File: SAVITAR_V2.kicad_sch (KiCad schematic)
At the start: 71 parts, among them IC1 CD4051BM_TR, IC2 CD4051BM_TR, J2 FH34SRJ-12S-0.5SH_50_

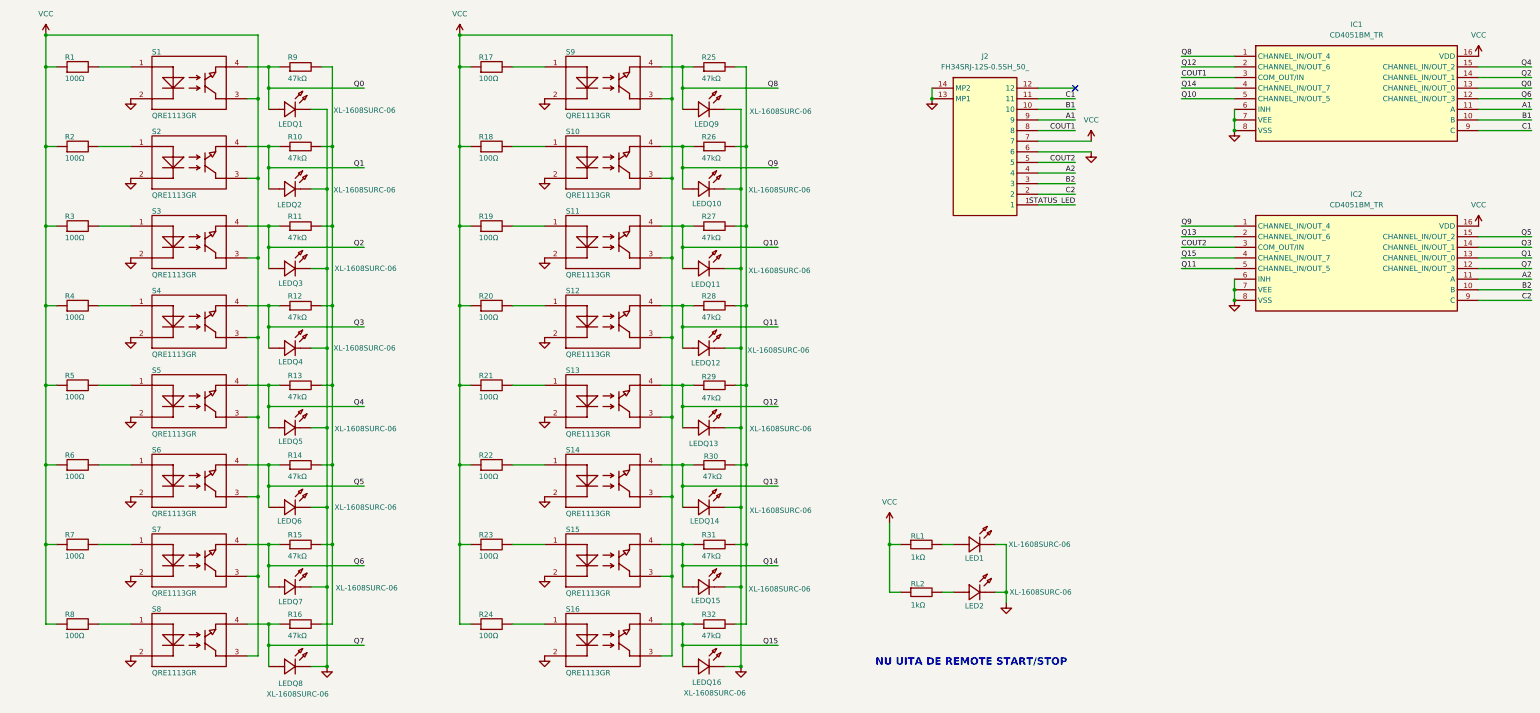
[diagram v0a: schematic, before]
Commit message: Added Decoder 3x8 (74HC238D) and 8 NMOS array (TBD62083AFNG) for driving the LEDs in pairs of 2 (±40 mA) only when they are read.
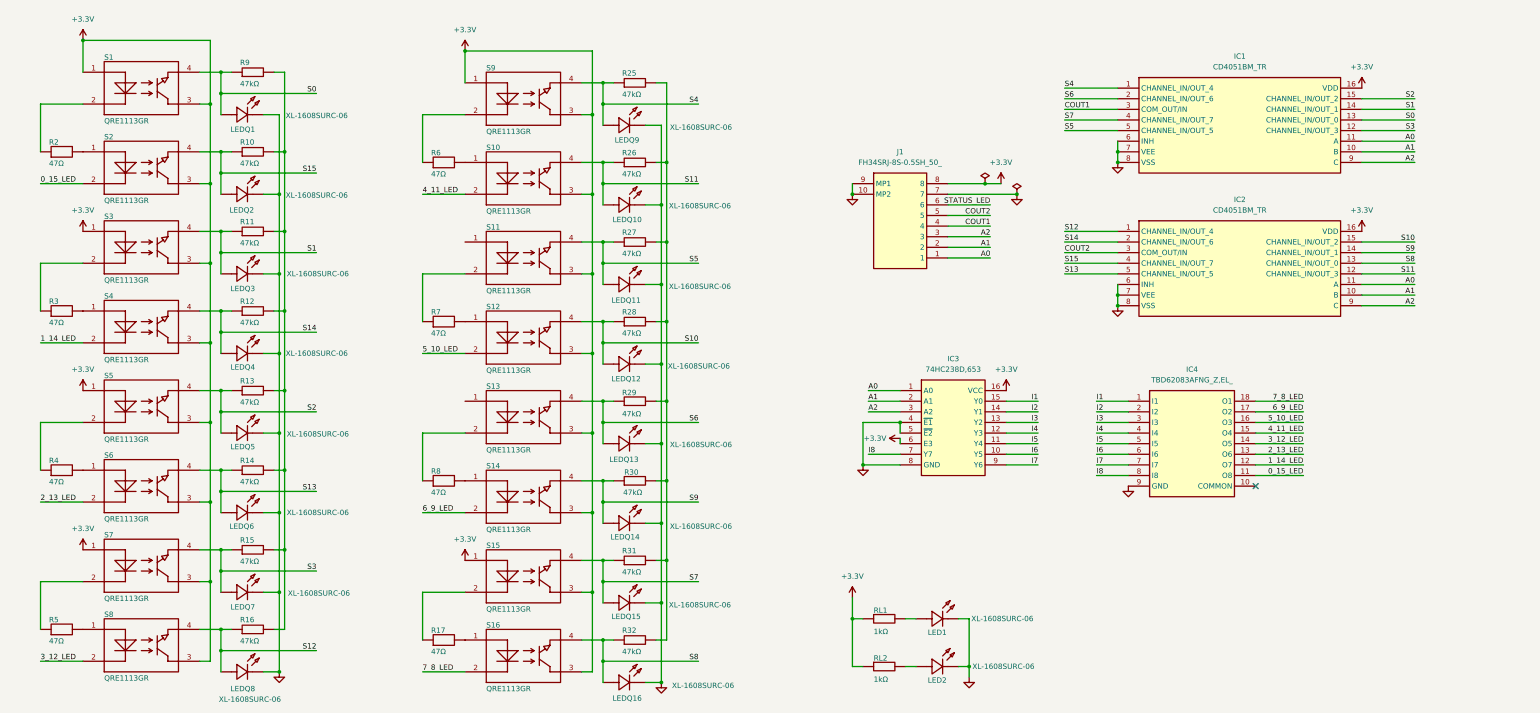
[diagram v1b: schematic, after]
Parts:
- removed J2: FH34SRJ-12S-0.5SH_50_, FH34SRJ-12S-0.5SH_50_:FH34SRJ12S05SH50, symbol FH34SRJ-12S-0_5SH_50_:FH34SRJ-12S-0.5SH_50_
- removed R1, R18, R19, R20, R21, R22, R23, R24: 100Ω, Resistor_SMD:R_0603_1608Metric, symbol SAVITAR_V2-altium-import:root_0_SCR0603J100R_
- added IC3: 74HC238D,653, 74HC238D653, symbol SAVITAR:74HC238D,653
- added IC4: TBD62083AFNG_Z,EL_, SOP65P640X155-18N, symbol SAVITAR:TBD62083AFNG_Z,EL_
- added J1: FH34SRJ-8S-0.5SH_50_, FH34SRJ8S05SH50, symbol SAVITAR:FH34SRJ-8S-0.5SH_50_
- R17, R2, R3, R4, R5, R6, R7, R8: value 100Ω -> 47Ω
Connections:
- net B1 is gone; now on net A1: IC1.10 (B)
- net B2 is gone; now on net A1: IC2.10 (B)
- net C1 is gone; now on net A2: IC1.9 (C)
- net C2 is gone; now on net A2: IC2.9 (C)
- net A1: now also IC3.2 (A1), J1.2; no longer IC1.11 (A)
- net A2: now also IC3.3 (A2), J1.3; no longer IC2.11 (A)
- net COUT1: now also J1.4
- net COUT2: now also J1.5
- net GND: now also IC3.4 (~{E1}), IC3.5 (~{E2}), IC3.8 (GND), IC4.9 (GND), J1.10 (MP2), J1.7, J1.9 (MP1); no longer S1.2, S10.2, S11.2, S12.2, S13.2, S14.2, S15.2, S16.2, S2.2, S3.2, S4.2, S5.2, S6.2, S7.2, S8.2, S9.2
- net STATUS_LED: now also J1.6
- net at R10.2, R11.2, R12.2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: now also R3.2; no longer R6.2
- net at R17.2: now also S16.1; no longer S9.1
- net at R5.2: now also S8.1; no longer S5.1
- net at R7.2: now also S12.1; no longer S7.1
- net +3.3V: now reaches S3.1
- net +3.3V: now also IC1.16 (VDD), IC2.16 (VDD), RL1.1, RL2.1, S1.1, S1.3, S10.3, S11.3, S12.3, S13.3, S14.3, S15.1, S15.3, S16.3, S2.3, S3.3, S4.3, S5.1, S5.3, S6.3, S7.1, S7.3, S8.3, S9.1, S9.3, IC3.16 (VCC), IC3.6 (E3), J1.8; no longer R3.2
- net at R8.2: now also S14.1; no longer S8.1
- net at S10.1: now also R6.2
- net Q0 renamed S0
- net Q1 renamed S15
- net S15: now also IC2.4 (CHANNEL_IN/OUT_7); no longer IC2.13 (CHANNEL_IN/OUT_0)
- net Q10 renamed S5
- net Q11 renamed S10
- net S10: now also IC2.15 (CHANNEL_IN/OUT_2); no longer IC2.5 (CHANNEL_IN/OUT_5)
- net Q12 renamed S6
- net Q13 renamed S9
- net S9: now also IC2.14 (CHANNEL_IN/OUT_1); no longer IC2.2 (CHANNEL_IN/OUT_6)
- net Q14 renamed S7
- net Q15 renamed S8
- net S8: now also IC2.13 (CHANNEL_IN/OUT_0); no longer IC2.4 (CHANNEL_IN/OUT_7)
- net Q2 renamed S1
- net Q3 renamed S14
- net S14: now also IC2.2 (CHANNEL_IN/OUT_6); no longer IC2.14 (CHANNEL_IN/OUT_1)
- net Q4 renamed S2
- net Q5 renamed S13
- net S13: now also IC2.5 (CHANNEL_IN/OUT_5); no longer IC2.15 (CHANNEL_IN/OUT_2)
- net Q6 renamed S3
- net Q7 renamed S12
- net S12: now also IC2.1 (CHANNEL_IN/OUT_4); no longer IC2.12 (CHANNEL_IN/OUT_3)
- net Q8 renamed S4
- net Q9 renamed S11
- net S11: now also IC2.12 (CHANNEL_IN/OUT_3); no longer IC2.1 (CHANNEL_IN/OUT_4)
- removed net VCC: IC1.16 (VDD), IC2.16 (VDD), R17.1, R2.1, R3.1, R4.1, R5.1, R6.1, R7.1, R8.1, RL1.1, RL2.1, S1.3, S10.3, S11.3, S12.3, S13.3, S14.3, S15.3, S16.3, S2.3, S3.3, S4.3, S5.3, S6.3, S7.3, S8.3, S9.3
- new net: R3.1, S3.2
- new net: R6.1, S9.2
- new net: R17.1, S15.2
- new net: R4.1, S5.2
- new net: R5.1, S7.2
- new net: R2.1, S1.2
- new net: R7.1, S11.2
- new net: R8.1, S13.2
- new net 0_15_LED: IC4.11 (O8), S2.2
- new net 1_14_LED: IC4.12 (O7), S4.2
- new net 2_13_LED: IC4.13 (O6), S6.2
- new net 3_12_LED: IC4.14 (O5), S8.2
- new net 4_11_LED: IC4.15 (O4), S10.2
- new net 5_10_LED: IC4.16 (O3), S12.2
- new net 6_9_LED: IC4.17 (O2), S14.2
- new net 7_8_LED: IC4.18 (O1), S16.2
- new net A0: IC1.11 (A), IC2.11 (A), IC3.1 (A0), J1.1
- new net I1: IC3.15 (Y0), IC4.1 (I1)
- new net I2: IC3.14 (Y1), IC4.2 (I2)
- new net I3: IC3.13 (Y2), IC4.3 (I3)
- new net I4: IC3.12 (Y3), IC4.4 (I4)
- new net I5: IC3.11 (Y4), IC4.5 (I5)
- new net I6: IC3.10 (Y5), IC4.6 (I6)
- new net I7: IC3.9 (Y6), IC4.7 (I7)
- new net I8: IC3.7 (Y7), IC4.8 (I8)
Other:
- note removed: "NU UITA DE REMOTE START/STOP"
- moved on the sheet: IC1, IC2, LED1, LED2, LEDQ1, LEDQ10, LEDQ11, LEDQ12, LEDQ13, LEDQ14, LEDQ15, LEDQ16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

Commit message: Changed schematic structure. Separated sensor array from PD processing and motor control. Sensor schematic is finished. Moving to MCU wiring. All project symbols and footprints are under SAVITAR name for easier finding. Add appropriate TAG.
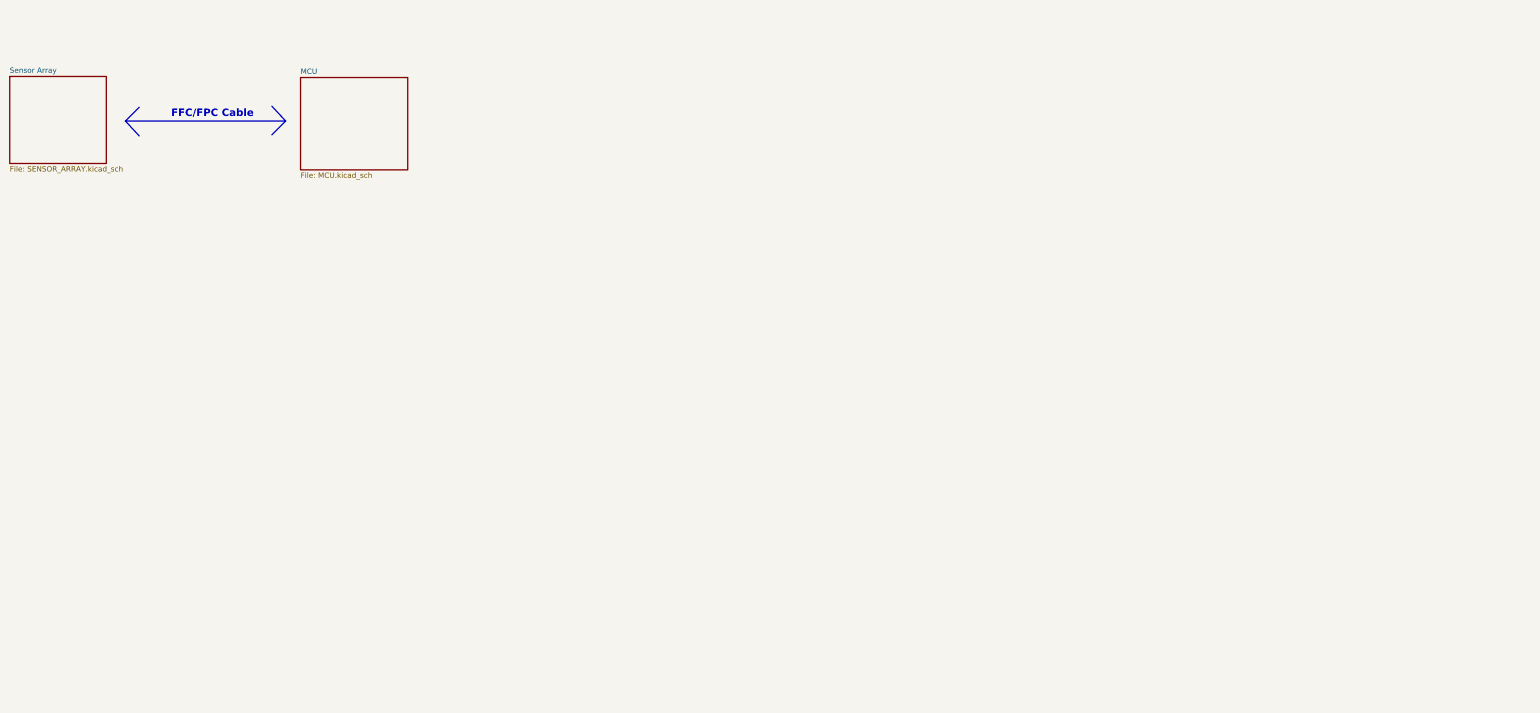
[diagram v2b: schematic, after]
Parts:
- removed IC1, IC2: CD4051BM_TR, CD4051BM_TR:SOIC127P602X182-16N, symbol CD4051BM_TR:CD4051BM_TR
- removed IC3: 74HC238D,653, 74HC238D653, symbol SAVITAR:74HC238D,653
- removed IC4: TBD62083AFNG_Z,EL_, SOP65P640X155-18N, symbol SAVITAR:TBD62083AFNG_Z,EL_
- removed J1: FH34SRJ-8S-0.5SH_50_, FH34SRJ8S05SH50, symbol SAVITAR:FH34SRJ-8S-0.5SH_50_
- removed LED1, LED2, LEDQ1, LEDQ10, LEDQ11, LEDQ12, LEDQ13, LEDQ14, LEDQ15, LEDQ16, LEDQ2, LEDQ3, LEDQ4, LEDQ5, LEDQ6, LEDQ7, LEDQ8, LEDQ9: XL-1608SURC-06, LED_SMD:LED_0603_1608Metric, symbol SAVITAR_V2-altium-import:root_0_mirrored_XL-1608SURC-06_
- removed R10, R11, R12, R13, R14, R15, R16, R25, R26, R27, R28, R29, R30, R31, R32, R9: 47kΩ, Resistor_SMD:R_0603_1608Metric, symbol SAVITAR_V2-altium-import:root_0_AC0603FR-0747KL_
- removed R17, R2, R3, R4, R5, R6, R7, R8: 47Ω, Resistor_SMD:R_0603_1608Metric, symbol SAVITAR_V2-altium-import:root_0_SCR0603J100R_
- removed RL1, RL2: 1kΩ, Resistor_SMD:R_0603_1608Metric, symbol SAVITAR_V2-altium-import:root_2_mirrored_RC0603FR-071KL_
- removed S1, S10, S11, S12, S13, S14, S15, S16, S2, S3, S4, S5, S6, S7, S8, S9: QRE1113GR, OptoDevice:OnSemi_CASE100CY, symbol SAVITAR_V2-altium-import:root_0_QRE1113GR_
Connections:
- no-connect marks 1 -> 0
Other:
- added sheet MCU (MCU.kicad_sch)
- added sheet Sensor Array (SENSOR_ARRAY.kicad_sch)
- note added: "FFC/FPC Cable"

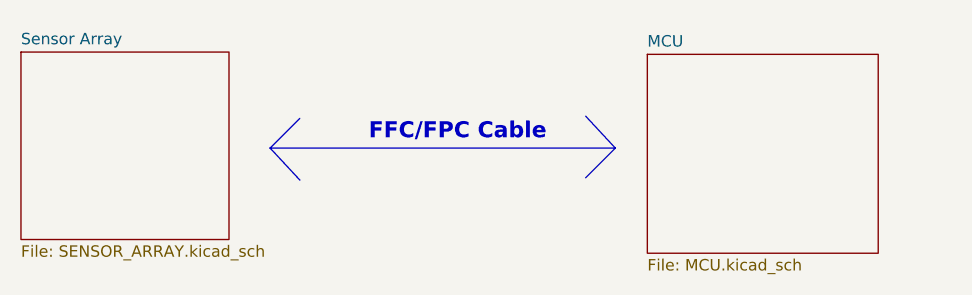
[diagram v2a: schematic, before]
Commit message: Changed motor driver from DRV8874 to a simpler, small-footprint DRV8837 using the IN1/IN2 interface.
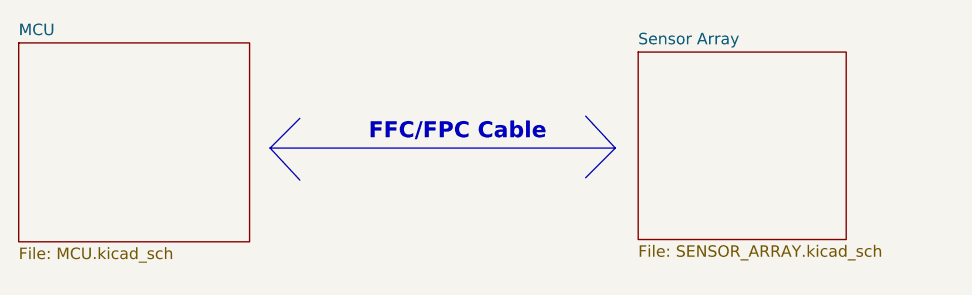
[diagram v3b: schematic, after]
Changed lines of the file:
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@@
 	)
 	(sheet
-		(at 88.9 36.83)
+		(at 19.05 35.56)
 		(size 25.654 22.098)
 		(exclude_from_sim no)
@@
 		)
 		(property "Sheetname" "MCU"
-			(at 88.9 36.1184 0)
+			(at 19.05 34.8484 0)
 			(show_name no)
 			(do_not_autoplace no)
@@
 		)
 		(property "Sheetfile" "MCU.kicad_sch"
-			(at 88.9 59.5126 0)
+			(at 19.05 58.2426 0)
 			(show_name no)
 			(do_not_autoplace no)
@@
 	)
 	(sheet
-		(at 19.304 36.576)
+		(at 87.884 36.576)
 		(size 23.114 20.828)
 		(exclude_from_sim no)
@@
 		)
 		(property "Sheetname" "Sensor Array"
-			(at 19.304 35.8644 0)
+			(at 87.884 35.8644 0)
 			(show_name no)
 			(do_not_autoplace no)
@@
 		)
 		(property "Sheetfile" "SENSOR_ARRAY.kicad_sch"
-			(at 19.304 57.9886 0)
+			(at 87.884 57.9886 0)
 			(show_name no)
 			(do_not_autoplace no)

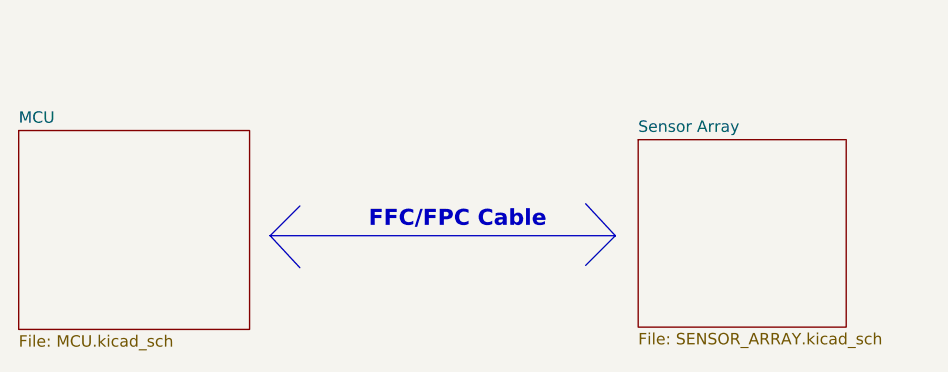
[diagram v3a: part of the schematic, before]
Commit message: Added ESP32-C3-MINI-1 circuit for the PD control over AP STA. Added comments and read sequence explanation. The schematic is finished, please add tag.
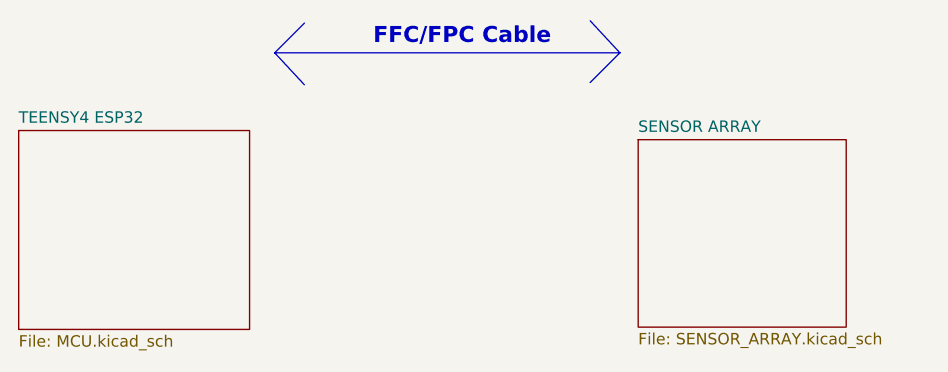
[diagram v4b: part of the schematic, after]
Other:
- sheet MCU renamed TEENSY4 ESP32
- sheet Sensor Array renamed SENSOR ARRAY
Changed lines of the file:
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@@
 	(text "FFC/FPC Cable "
 		(exclude_from_sim no)
-		(at 67.818 45.466 0)
+		(at 68.326 25.146 0)
 		(effects
 			(font
@@
 	(polyline
 		(pts
-			(xy 50.292 50.8) (xy 46.99 47.244)
+			(xy 50.8 30.48) (xy 47.498 26.924)
 		)
 		(stroke
@@
 	(polyline
 		(pts
-			(xy 50.292 43.942) (xy 46.99 47.244)
+			(xy 50.8 23.622) (xy 47.498 26.924)
 		)
 		(stroke
@@
 	(polyline
 		(pts
-			(xy 82.042 43.688) (xy 85.344 47.244)
+			(xy 82.55 23.368) (xy 85.852 26.924)
 		)
 		(stroke
@@
 	(polyline
 		(pts
-			(xy 82.042 50.546) (xy 85.344 47.244)
+			(xy 82.55 30.226) (xy 85.852 26.924)
 		)
 		(stroke
@@
 	(polyline
 		(pts
-			(xy 46.99 47.244) (xy 85.344 47.244)
+			(xy 47.498 26.924) (xy 85.852 26.924)
 		)
 		(stroke
@@
 			(color 0 0 0 0)
 		)
-		(property "Sheetname" "MCU"
+		(property "Sheetname" "TEENSY4 ESP32"
 			(at 19.05 34.8484 0)
 			(show_name no)
@@
 			(project "SAVITAR_V2"
 				(path "/f6d97783-3721-4b78-8f0f-ed81f34e7161"
-					(page "3")
+					(page "2")
 				)
 			)
@@
 			(color 0 0 0 0)
 		)
-		(property "Sheetname" "Sensor Array"
+		(property "Sheetname" "SENSOR ARRAY"
 			(at 87.884 35.8644 0)
 			(show_name no)
@@
 			(project "SAVITAR_V2"
 				(path "/f6d97783-3721-4b78-8f0f-ed81f34e7161"
-					(page "2")
+					(page "3")
 				)
 			)
